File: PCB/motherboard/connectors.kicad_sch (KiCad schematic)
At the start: 12 parts, among them J1 Conn_01x04, J10 Screw_Terminal_01x03, J11 Conn_01x05, J12 Conn_01x11, J13 Conn_01x03, J2 Conn_01x06, J3 Conn_01x08, J4 Conn_01x04, J5 Conn_01x03, J6 Conn_01x03, J8 Conn_01x06, J9 Conn_01x02

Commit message: pcb layout
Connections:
- net +24V renamed +24V_UNPROTECTED
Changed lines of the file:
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@@
 			)
 		)
-		(property "Value" "+24V"
-			(at 237.49 43.1799 90)
+		(property "Value" "+24V_UNPROTECTED"
+			(at 240.03 40.64 90)
 			(show_name no)
 			(do_not_autoplace no)
@@
 					(size 1.27 1.27)
 				)
-				(justify left)
 			)
 		)

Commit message: pcb layout : collegamento piste + vie + cambio connettori
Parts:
- J10: footprint TerminalBlock_Phoenix:TerminalBlock_Phoenix_MPT-0,5-3-2.54_1x03_P2.54mm_Horizontal -> TerminalBlock_Phoenix:TerminalBlock_Phoenix_PT-1,5-3-5.0-H_1x03_P5.00mm_Horizontal
- J4: footprint TerminalBlock_Phoenix:TerminalBlock_Phoenix_MPT-0,5-4-2.54_1x04_P2.54mm_Horizontal -> Connector_PinSocket_2.54mm:PinSocket_1x04_P2.54mm_Vertical
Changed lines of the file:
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@@
 			)
 		)
-		(property "Footprint" "TerminalBlock_Phoenix:TerminalBlock_Phoenix_MPT-0,5-4-2.54_1x04_P2.54mm_Horizontal"
+		(property "Footprint" "Connector_PinSocket_2.54mm:PinSocket_1x04_P2.54mm_Vertical"
 			(at 63.5 147.32 0)
 			(hide yes)
@@
 			)
 		)
-		(property "Footprint" "TerminalBlock_Phoenix:TerminalBlock_Phoenix_MPT-0,5-3-2.54_1x03_P2.54mm_Horizontal"
+		(property "Footprint" "TerminalBlock_Phoenix:TerminalBlock_Phoenix_PT-1,5-3-5.0-H_1x03_P5.00mm_Horizontal"
 			(at 260.35 86.36 0)
 			(hide yes)

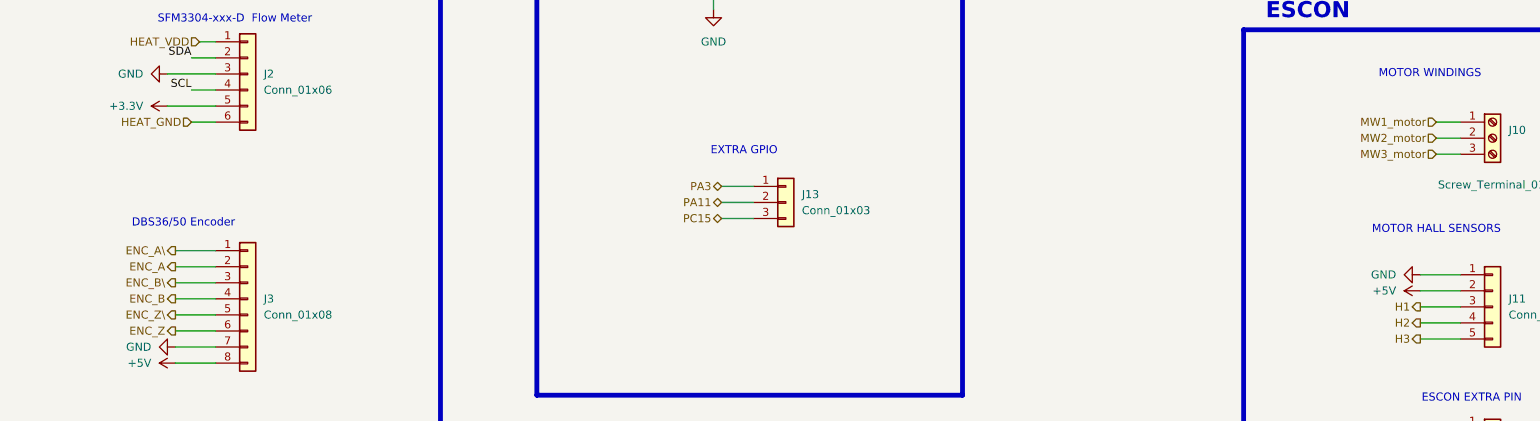
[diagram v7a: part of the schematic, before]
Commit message: resolved pcb errors from drc, generated test output files
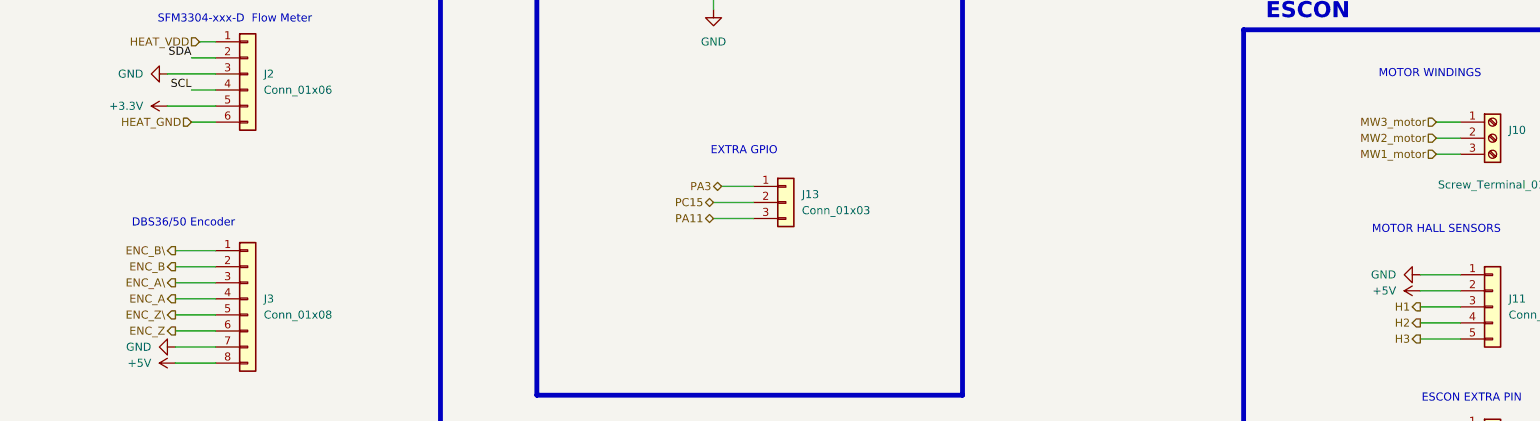
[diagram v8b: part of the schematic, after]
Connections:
- net ENC_A: now also J3.4 (Pin_4); no longer J3.2 (Pin_2)
- net ENC_A\: now also J3.3 (Pin_3); no longer J3.1 (Pin_1)
- net ENC_B: now also J3.2 (Pin_2); no longer J3.4 (Pin_4)
- net ENC_B\: now also J3.1 (Pin_1); no longer J3.3 (Pin_3)
- net MW1_motor: now also J10.3 (Pin_3); no longer J10.1 (Pin_1)
- net MW3_motor: now also J10.1 (Pin_1); no longer J10.3 (Pin_3)
- net PA11: now also J13.3 (Pin_3); no longer J13.2 (Pin_2)
- net PC15: now also J13.2 (Pin_2); no longer J13.3 (Pin_3)
